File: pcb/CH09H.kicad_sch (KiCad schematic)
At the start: 5 parts

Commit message: Corrections to the coax driver
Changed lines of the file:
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@@
     (effects (font (size 1.27 1.27)) (justify right))
   )
-  (symbol (lib_id "Transistor_BJT:BC856BS") (at 106.68 52.07 0) (mirror x)
+  (symbol (lib_id "Transistor_BJT:BC856BS") (at 106.68 52.07 0) (mirror x) (unit 1)
     (in_bom yes) (on_board yes)
     (property "Reference" "Q?" (id 0) (at 111.506 53.2384 0)
@@
     (pin "6")
   )
-  (symbol (lib_id "Connector:Conn_Coaxial") (at 116.84 63.5 0)
+  (symbol (lib_id "Connector:Conn_Coaxial") (at 116.84 63.5 0) (unit 1)
     (in_bom yes) (on_board yes)
     (property "Reference" "J?" (id 0) (at 119.38 64.135 0)
@@
     (pin "2")
   )
-  (symbol (lib_id "Device:R") (at 93.98 52.07 270)
+  (symbol (lib_id "Device:R") (at 93.98 52.07 270) (unit 1)
     (in_bom yes) (on_board yes)
     (property "Reference" "R?" (id 0) (at 93.98 46.8122 90))
@@
     (pin "2")
   )
-  (symbol (lib_id "Device:R") (at 116.84 78.74 0)
+  (symbol (lib_id "Device:R") (at 116.84 78.74 0) (unit 1)
     (in_bom yes) (on_board yes)
     (property "Reference" "R?" (id 0) (at 118.618 77.5716 0)
@@
     (pin "2")
   )
-  (symbol (lib_id "power:GND") (at 116.84 96.52 0)
+  (symbol (lib_id "power:GND") (at 116.84 96.52 0) (unit 1)
     (in_bom yes) (on_board yes)
     (property "Reference" "#PWR?" (id 0) (at 116.84 102.87 0)
@@
     (pin "1")
   )
-  (symbol (lib_id "Device:R") (at 116.84 90.17 0)
+  (symbol (lib_id "Device:R") (at 116.84 90.17 0) (unit 1)
     (in_bom yes) (on_board yes)
     (property "Reference" "R?" (id 0) (at 118.618 89.0016 0)

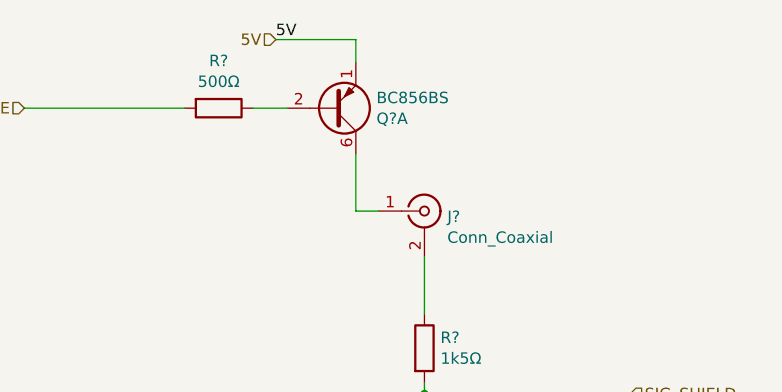
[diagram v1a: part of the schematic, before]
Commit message: Shift register updates - changes the driver from pnp to npn
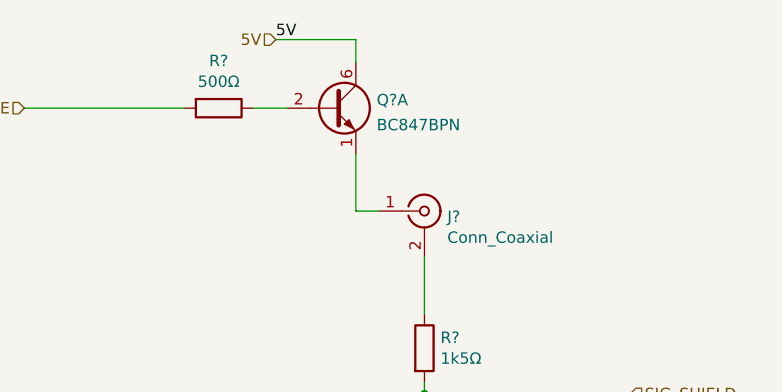
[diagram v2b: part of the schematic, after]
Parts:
- removed Q?: BC856BS, Package_TO_SOT_SMD:SOT-363_SC-70-6, symbol Transistor_BJT:BC856BS
- added Q?: BC847BPN, Package_TO_SOT_SMD:SOT-363_SC-70-6, symbol Transistor_BJT:BC847BPN
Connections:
- net 5V: now also Q?.6 (C1)
- net at R?.1: now also Q?.2 (B1)
- net at J?.1 (In): now also Q?.1 (E1)
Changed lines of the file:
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@@
     (effects (font (size 1.27 1.27)) (justify right))
-  )
-  (symbol (lib_id "Transistor_BJT:BC856BS") (at 106.68 52.07 0) (mirror x) (unit 1)
-    (in_bom yes) (on_board yes)
-    (property "Reference" "Q?" (id 0) (at 111.506 53.2384 0)
-      (effects (font (size 1.27 1.27)) (justify left))
-    )
-    (property "Value" "BC856BS" (id 1) (at 111.506 50.927 0)
-      (effects (font (size 1.27 1.27)) (justify left))
-    )
-    (property "Footprint" "Package_TO_SOT_SMD:SOT-363_SC-70-6" (id 2) (at 111.76 54.61 0)
-      (effects (font (size 1.27 1.27)) hide)
-    )
-    (property "Datasheet" "https://assets.nexperia.com/documents/data-sheet/BC856BS.pdf" (id 3) (at 106.68 52.07 0)
-      (effects (font (size 1.27 1.27)) hide)
-    )
-    (pin "1")
-    (pin "2")
-    (pin "6")
   )
   (symbol (lib_id "Connector:Conn_Coaxial") (at 116.84 63.5 0) (unit 1)
@@
     (pin "2")
   )
+  (symbol (lib_id "Transistor_BJT:BC847BPN") (at 106.68 52.07 0) (unit 1)
+    (in_bom yes) (on_board yes) (fields_autoplaced)
+    (property "Reference" "Q?" (id 0) (at 111.5314 51.1615 0)
+      (effects (font (size 1.27 1.27)) (justify left))
+    )
+    (property "Value" "BC847BPN" (id 1) (at 111.5314 53.9366 0)
+      (effects (font (size 1.27 1.27)) (justify left))
+    )
+    (property "Footprint" "Package_TO_SOT_SMD:SOT-363_SC-70-6" (id 2) (at 111.76 49.53 0)
+      (effects (font (size 1.27 1.27)) hide)
+    )
+    (property "Datasheet" "https://assets.nexperia.com/documents/data-sheet/BC847BPN.pdf" (id 3) (at 106.68 52.07 0)
+      (effects (font (size 1.27 1.27)) hide)
+    )
+    (pin "1")
+    (pin "2")
+    (pin "6")
+  )
 )

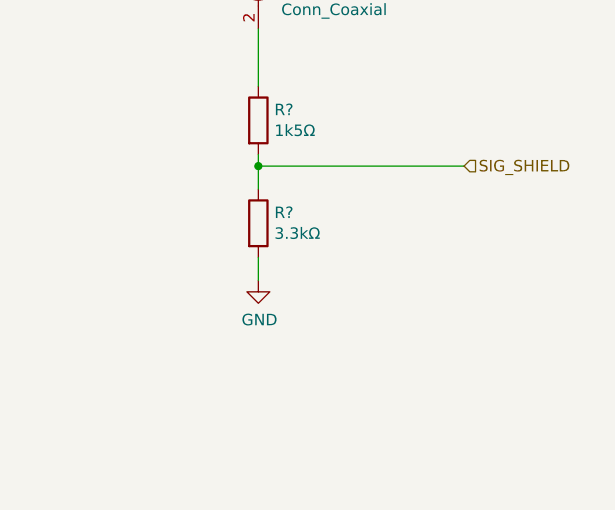
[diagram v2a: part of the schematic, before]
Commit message: Adds line protection
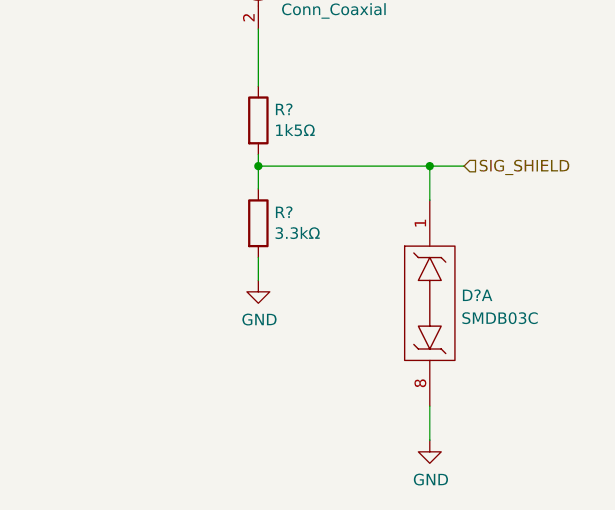
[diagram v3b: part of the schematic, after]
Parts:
- added D?: SMDB03C, Package_SO:SO-8_3.9x4.9mm_P1.27mm, symbol CoaxTester:SMDB03C
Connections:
- net GND: now also D?.8
- net SIG_SHIELD: now also D?.1
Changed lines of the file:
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@@
 (kicad_sch (version 20211123) (generator eeschema)
   (paper "A4")
+  (junction (at 135.89 83.82) (diameter 0) (color 0 0 0 0)
+  )
   (junction (at 116.84 83.82) (diameter 0) (color 0 0 0 0)
   )
   (wire (pts (xy 116.84 68.58) (xy 116.84 74.93))
+    (stroke (width 0) (type default) (color 0 0 0 0))
+  )
+  (wire (pts (xy 135.89 110.49) (xy 135.89 114.3))
     (stroke (width 0) (type default) (color 0 0 0 0))
   )
@@
     (stroke (width 0) (type default) (color 0 0 0 0))
   )
+  (wire (pts (xy 135.89 83.82) (xy 135.89 87.63))
+    (stroke (width 0) (type default) (color 0 0 0 0))
+  )
   (wire (pts (xy 109.22 46.99) (xy 109.22 44.45))
+    (stroke (width 0) (type default) (color 0 0 0 0))
+  )
+  (wire (pts (xy 135.89 83.82) (xy 139.7 83.82))
     (stroke (width 0) (type default) (color 0 0 0 0))
   )
@@
     (stroke (width 0) (type default) (color 0 0 0 0))
   )
-  (wire (pts (xy 116.84 83.82) (xy 139.7 83.82))
+  (wire (pts (xy 116.84 83.82) (xy 135.89 83.82))
     (stroke (width 0) (type default) (color 0 0 0 0))
   )
@@
     (pin "2")
   )
+  (symbol (lib_id "CoaxTester:SMDB03C") (at 135.89 99.06 0) (unit 1)
+    (in_bom yes) (on_board yes) (fields_autoplaced)
+    (property "Reference" "D?" (id 0) (at 139.3952 98.2253 0)
+      (effects (font (size 1.27 1.27)) (justify left))
+    )
+    (property "Value" "SMDB03C" (id 1) (at 139.3952 100.7622 0)
+      (effects (font (size 1.27 1.27)) (justify left))
+    )
+    (property "Footprint" "Package_SO:SO-8_3.9x4.9mm_P1.27mm" (id 2) (at 135.89 97.79 0)
+      (effects (font (size 1.27 1.27)) hide)
+    )
+    (property "Datasheet" "https://www.smc-diodes.com/propdf/SMDB03C%20THRU%20SMDB24C%20N0426%20REV.A.pdf" (id 3) (at 135.89 97.79 0)
+      (effects (font (size 1.27 1.27)) hide)
+    )
+    (pin "1")
+    (pin "8")
+  )
   (symbol (lib_id "Transistor_BJT:BC847BPN") (at 106.68 52.07 0) (unit 1)
     (in_bom yes) (on_board yes) (fields_autoplaced)
@@
     (pin "6")
   )
+  (symbol (lib_id "power:GND") (at 135.89 114.3 0) (unit 1)
+    (in_bom yes) (on_board yes)
+    (property "Reference" "#PWR?" (id 0) (at 135.89 120.65 0)
+      (effects (font (size 1.27 1.27)) hide)
+    )
+    (property "Value" "GND" (id 1) (at 136.017 118.6942 0))
+    (property "Footprint" "" (id 2) (at 135.89 114.3 0)
+      (effects (font (size 1.27 1.27)) hide)
+    )
+    (property "Datasheet" "" (id 3) (at 135.89 114.3 0)
+      (effects (font (size 1.27 1.27)) hide)
+    )
+    (pin "1")
+  )
 )

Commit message: Schematic complete
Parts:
- gave numbers to parts that had none: 6
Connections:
- net 5V renamed +5V
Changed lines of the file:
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@@
-    (stroke (width 0) (type default) (color 0 0 0 0))
-  )
-  (wire (pts (xy 109.22 44.45) (xy 100.33 44.45))
     (stroke (width 0) (type default) (color 0 0 0 0))
   )
@@
     (stroke (width 0) (type default) (color 0 0 0 0))
   )
-  (label "5V" (at 100.33 44.45 0)
-    (effects (font (size 1.27 1.27)) (justify left bottom))
-  )
-  (hierarchical_label "5V" (shape input) (at 100.33 44.45 180)
-    (effects (font (size 1.27 1.27)) (justify right))
-  )
   (hierarchical_label "SIG_SHIELD" (shape input) (at 139.7 83.82 0)
     (effects (font (size 1.27 1.27)) (justify left))
@@
   (symbol (lib_id "Connector:Conn_Coaxial") (at 116.84 63.5 0) (unit 1)
     (in_bom yes) (on_board yes)
-    (property "Reference" "J?" (id 0) (at 119.38 64.135 0)
+    (property "Reference" "J601" (id 0) (at 119.38 64.135 0)
       (effects (font (size 1.27 1.27)) (justify left))
     )
@@
   (symbol (lib_id "Device:R") (at 93.98 52.07 270) (unit 1)
     (in_bom yes) (on_board yes)
-    (property "Reference" "R?" (id 0) (at 93.98 46.8122 90))
+    (property "Reference" "R601" (id 0) (at 93.98 46.8122 90))
     (property "Value" "500Ω" (id 1) (at 93.98 49.1236 90))
     (property "Footprint" "Resistor_SMD:R_0805_2012Metric" (id 2) (at 93.98 50.292 90)
@@
   (symbol (lib_id "Device:R") (at 116.84 78.74 0) (unit 1)
     (in_bom yes) (on_board yes)
-    (property "Reference" "R?" (id 0) (at 118.618 77.5716 0)
+    (property "Reference" "R602" (id 0) (at 118.618 77.5716 0)
       (effects (font (size 1.27 1.27)) (justify left))
     )
@@
   (symbol (lib_id "power:GND") (at 116.84 96.52 0) (unit 1)
     (in_bom yes) (on_board yes)
-    (property "Reference" "#PWR?" (id 0) (at 116.84 102.87 0)
+    (property "Reference" "#PWR0602" (id 0) (at 116.84 102.87 0)
       (effects (font (size 1.27 1.27)) hide)
     )
@@
   (symbol (lib_id "Device:R") (at 116.84 90.17 0) (unit 1)
     (in_bom yes) (on_board yes)
-    (property "Reference" "R?" (id 0) (at 118.618 89.0016 0)
+    (property "Reference" "R603" (id 0) (at 118.618 89.0016 0)
       (effects (font (size 1.27 1.27)) (justify left))
     )
@@
     (pin "2")
   )
+  (symbol (lib_id "power:+5V") (at 109.22 44.45 0) (unit 1)
+    (in_bom yes) (on_board yes) (fields_autoplaced)
+    (property "Reference" "#PWR0601" (id 0) (at 109.22 48.26 0)
+      (effects (font (size 1.27 1.27)) hide)
+    )
+    (property "Value" "+5V" (id 1) (at 109.22 40.8742 0))
+    (property "Footprint" "" (id 2) (at 109.22 44.45 0)
+      (effects (font (size 1.27 1.27)) hide)
+    )
+    (property "Datasheet" "" (id 3) (at 109.22 44.45 0)
+      (effects (font (size 1.27 1.27)) hide)
+    )
+    (pin "1")
+  )
   (symbol (lib_id "CoaxTester:SMDB03C") (at 135.89 99.06 0) (unit 1)
     (in_bom yes) (on_board yes) (fields_autoplaced)
-    (property "Reference" "D?" (id 0) (at 139.3952 98.2253 0)
+    (property "Reference" "D601" (id 0) (at 139.3952 98.2253 0)
       (effects (font (size 1.27 1.27)) (justify left))
     )
@@
     (pin "1")
     (pin "8")
+    (pin "2")
+    (pin "7")
+    (pin "3")
+    (pin "6")
+    (pin "4")
+    (pin "5")
   )
   (symbol (lib_id "Transistor_BJT:BC847BPN") (at 106.68 52.07 0) (unit 1)
     (in_bom yes) (on_board yes) (fields_autoplaced)
-    (property "Reference" "Q?" (id 0) (at 111.5314 51.1615 0)
+    (property "Reference" "Q601" (id 0) (at 111.5314 51.1615 0)
       (effects (font (size 1.27 1.27)) (justify left))
     )
@@
     (pin "2")
     (pin "6")
+    (pin "3")
+    (pin "4")
+    (pin "5")
   )
   (symbol (lib_id "power:GND") (at 135.89 114.3 0) (unit 1)
     (in_bom yes) (on_board yes)
-    (property "Reference" "#PWR?" (id 0) (at 135.89 120.65 0)
+    (property "Reference" "#PWR0603" (id 0) (at 135.89 120.65 0)
       (effects (font (size 1.27 1.27)) hide)
     )

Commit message: DRC OK
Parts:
- added unit 2 of D601
- added unit 4 of D601
- added unit 3 of D601
- added unit 2 of Q601
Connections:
- no-connect marks 0 -> 9
